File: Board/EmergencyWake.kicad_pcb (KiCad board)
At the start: 2 copper layers, 100 x 67 mm, 128 parts, among them J1 USB_C_Plug_USB2.0, J2 Micro_SD_Card_Det, J3 Conn_01x03, J4 Conn_01x02, J5 Conn_01x03, J6 Conn_01x04, J7 Conn_01x02, J8 Conn_01x04, J9 Conn_01x04, Q1 AO3400A, Q2 AO3401A, SW1 SW_DPDT_x2, SW2 SW_Push, SW3 SW_Push, SW4 SW_Push, U1 M24C02-WMN, U10 L9110S, U2 AMS1117-3.3, U3 MC34063AD, U4 STM32F103VETx, U5 LM4670, U6 173950378, U7 PT6312B, U8 EL357N-G, U9 EL357N-G, Y1 32,768

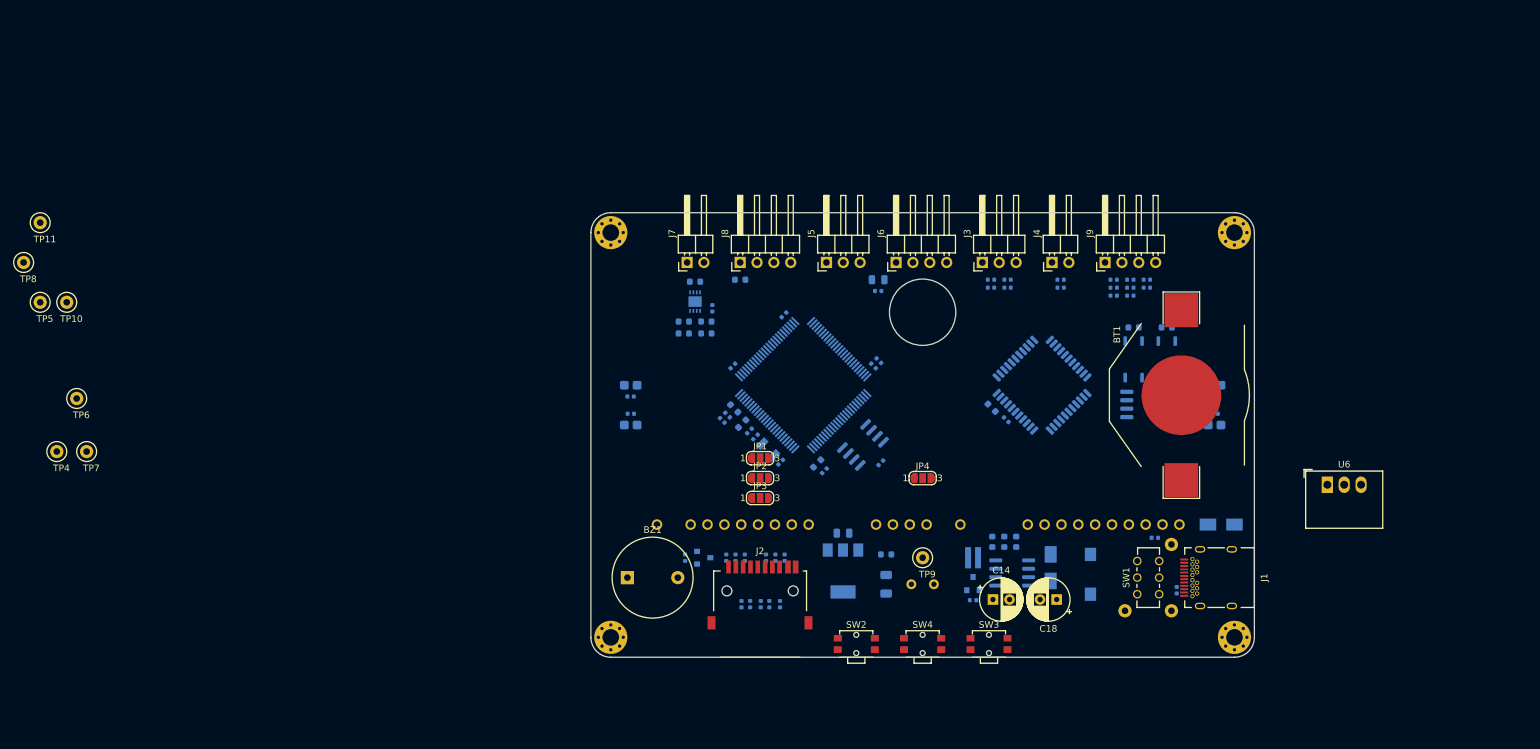
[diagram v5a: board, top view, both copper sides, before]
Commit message: [Board] Moved all components to the front of the board
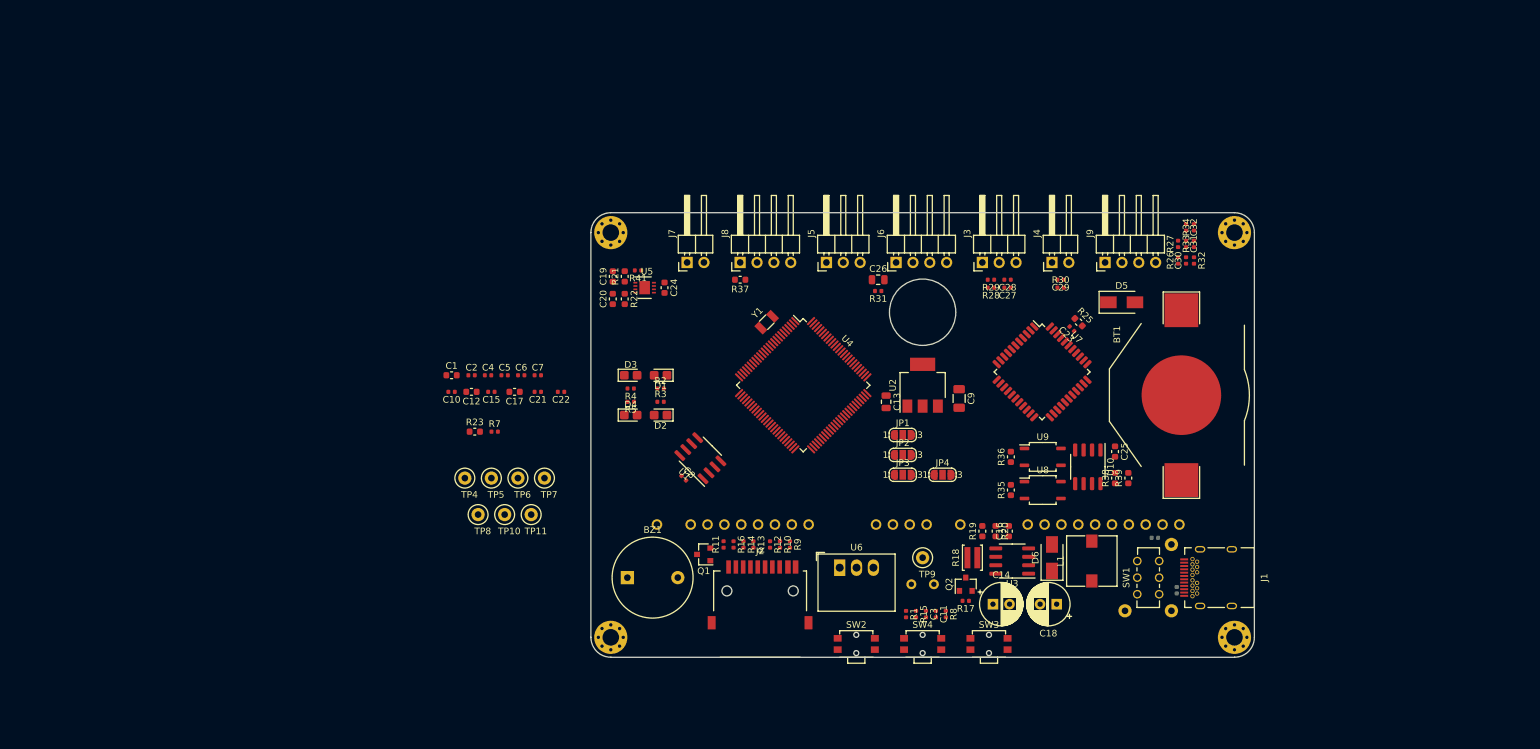
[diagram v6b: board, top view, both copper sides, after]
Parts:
- C1, C10, C11, C12, C13, C15, C16, C17, C19, C2, C20, C21, C22, C23, C24, C25, C26, C27, C28, C29, C3, C30, C31, C32, C4, C5, C6, C7, C8, C9, D1, D2, D3, D4, D5, D6, L1, Q1, Q2, R1, R10, R11, R12, R13, R14, R15, R16, R17, R18, R19, R2, R20, R21, R22, R23, R25, R26, R27, R28, R29, R3, R30, R31, R32, R33, R34, R35, R36, R37, R38, R39, R4, R41, R5, R7, R8, R9, U1, U10, U2, U3, U4, U5, U7, U8, U9, Y1: moved to F.Cu
- moved R5 88.0 mm to (106.0, 128.5), turned to 180 degrees
- moved D3 88.0 mm to (106.0, 124.5), turned to 0 degrees
- moved D4 88.0 mm to (106.0, 130.5), turned to 0 degrees
- moved R4 88.0 mm to (106.0, 126.5), turned to 180 degrees
- moved TP11 86.1 mm to (91.0, 145.5)
- moved TP8 78.3 mm to (83.0, 145.5)
- moved U6 74.6 mm to (137.5, 153.5)
- moved TP10 73.3 mm to (87.0, 145.5)
- moved TP5 73.0 mm to (85.0, 140.0)
- moved TP7 69.1 mm to (93.0, 140.0)
- moved TP6 67.6 mm to (89.0, 140.0)
- moved R23 64.7 mm to (82.5, 133.0)
- moved TP4 61.6 mm to (81.0, 140.0)
- moved R7 58.9 mm to (85.5, 133.0), turned to 0 degrees
- moved C1 56.7 mm to (79.0, 124.5), turned to 0 degrees
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
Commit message: [Board] Finished moving components to front of board
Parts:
- R40, R6, TP1, TP2, TP3: moved to F.Cu
- moved TP10 88.7 mm to (174.5, 131.0)
- moved TP11 69.8 mm to (156.0, 120.0)
- moved TP5 68.1 mm to (152.0, 152.0)
- moved TP4 66.1 mm to (144.0, 120.0)
- moved R7 55.7 mm to (141.1, 130.4), turned to 225 degrees
- moved TP8 55.1 mm to (138.0, 148.0)
- moved C6 53.3 mm to (142.6, 128.9), turned to 225 degrees
- moved C1 45.6 mm to (124.2, 118.8), turned to 135 degrees
- moved C7 43.9 mm to (134.9, 115.4), turned to 315 degrees
- moved C5 43.8 mm to (129.1, 136.6), turned to 135 degrees
- moved C2 43.7 mm to (125.2, 117.8), turned to 135 degrees
- moved C10 41.1 mm to (119.8, 122.3), turned to 225 degrees
- moved R23 40.7 mm to (123.2, 131.1), turned to 315 degrees
- moved C12 39.0 mm to (120.8, 123.3), turned to 225 degrees
- moved TP7 38.9 mm to (109.0, 104.5)
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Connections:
- D5 pad 1: Net-(D5-Pad1) -> VCC
- D5 pad 2: +3V0 -> Net-(D5-Pad2)
- SW1 pad 4: VCC -> Net-(D5-Pad2)
- SW1 pad 5: Net-(D5-Pad1) -> +3V0
- TP11 pad 1: /DCF_PON -> /DCF_SIG

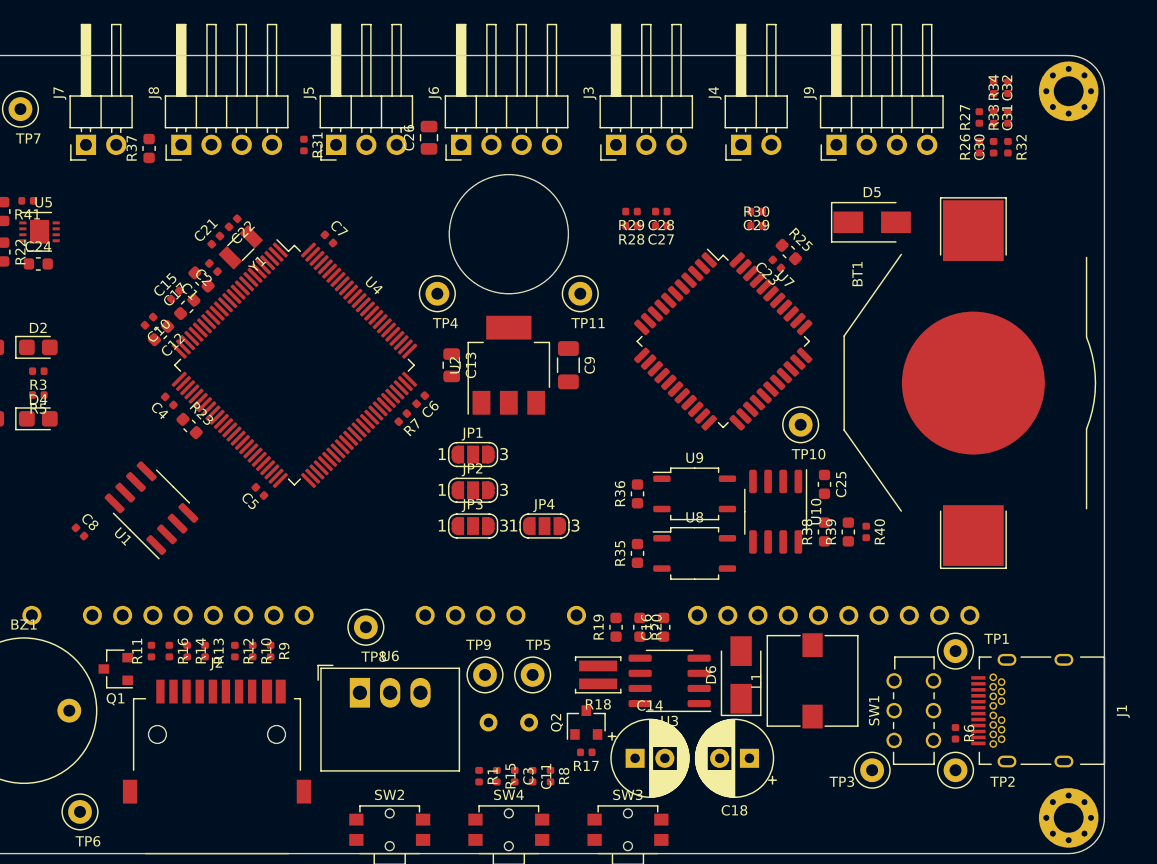
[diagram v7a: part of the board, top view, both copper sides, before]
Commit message: [Board] Checked schematic for errors
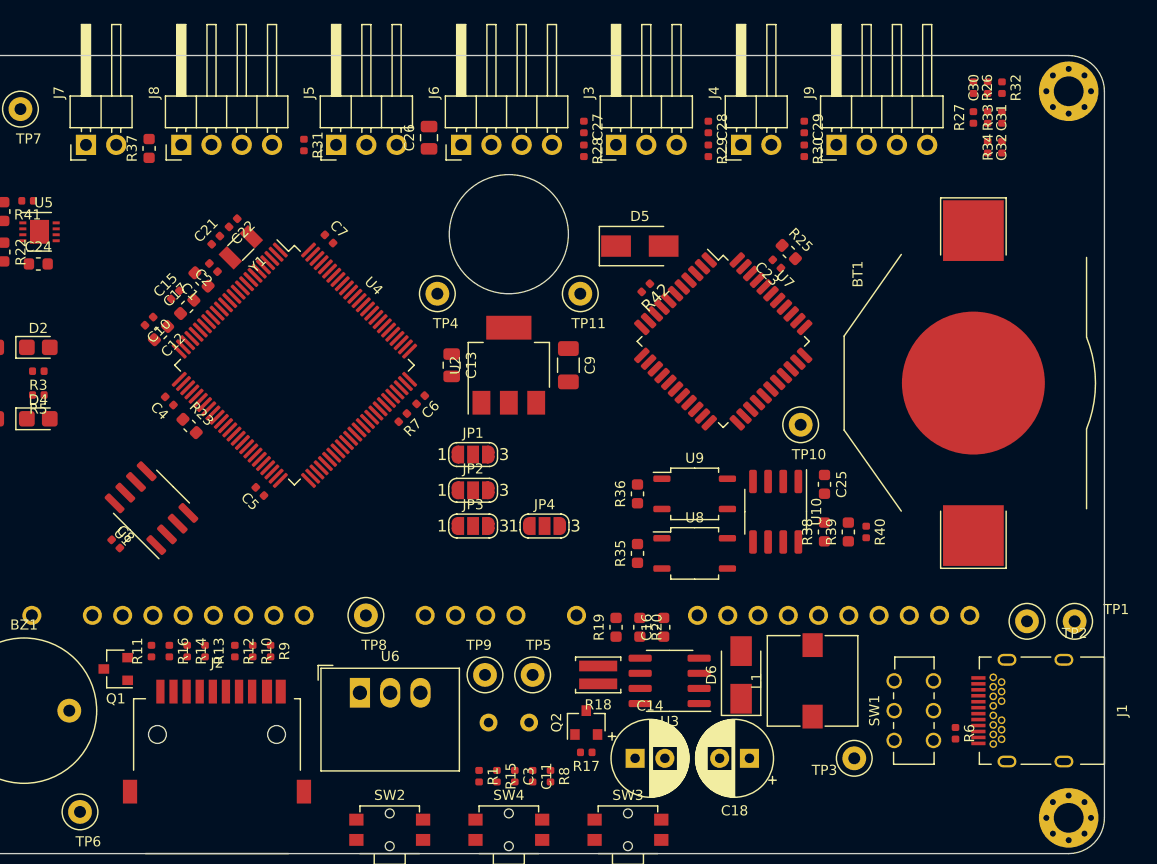
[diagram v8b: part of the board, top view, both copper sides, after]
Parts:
- added R42: 100k, Resistor_SMD:R_0402_1005Metric, F.Cu at (161.5, 119.5)
- R25: value R -> 51k
- moved D5 19.6 mm to (161.0, 116.0)
- moved TP2 13.9 mm to (193.5, 147.5)
- moved C27 10.5 mm to (156.3, 106.0), turned to 270 degrees
- moved TP1 10.3 mm to (197.5, 147.5)
- moved R29 8.22 mm to (166.8, 108.0), turned to 270 degrees
- moved C29 8.15 mm to (174.8, 106.0), turned to 270 degrees
- moved C28 8.12 mm to (166.8, 106.0), turned to 270 degrees
- moved R28 7.46 mm to (156.3, 108.0), turned to 270 degrees
- moved R30 7.46 mm to (174.8, 108.0), turned to 270 degrees
- moved C30 5.02 mm to (190.2, 102.7)
- moved C32 5.02 mm to (190.2, 107.7)
- moved R26 5.02 mm to (189.0, 102.7), turned to 270 degrees
- moved R32 5.02 mm to (191.4, 102.7)
- moved R34 5.02 mm to (191.4, 107.7)
- moved C8 3.16 mm to (117.0, 141.0)
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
